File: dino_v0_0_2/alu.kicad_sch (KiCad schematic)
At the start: 20 parts, among them U38 74F382N, U40 74F382N, U45 74LS373, U46 74LS373, U47 74LS373, U48 74LS157, U49 74LS273, U50 74LS02, U52 74LS02, U53 74LS08

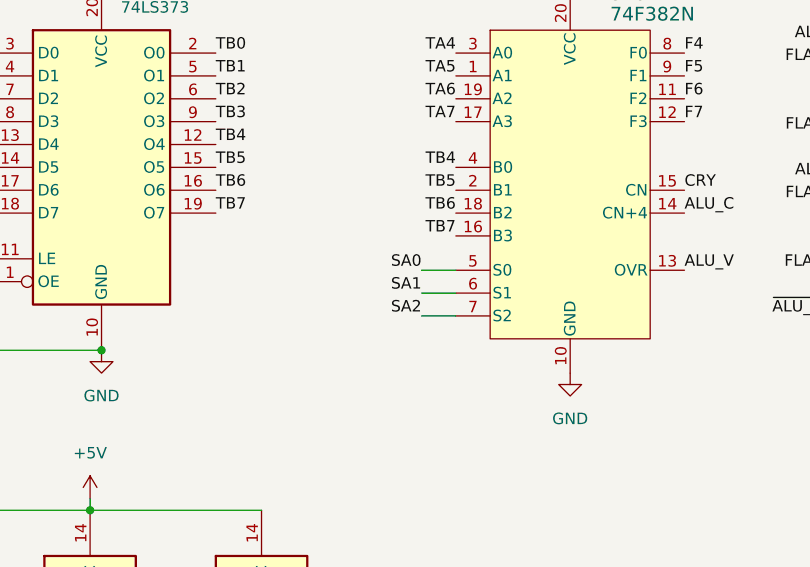
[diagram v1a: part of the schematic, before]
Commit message: schematic: join five aliased nets, and ledger the root-sheet gap
FIVE LIVE WIRES WERE IN THE CHECKLIST'S NO-CONNECT BUCKET, under the
heading "nothing to land and nothing to beep against."

  CW9/SA2           U15.12  <->  U38.7, U40.7
  CW10/SA1          U15.13  <->  U38.6, U40.6, U53.12
  CW11/SA0          U15.15  <->  U38.5, U40.5, U53.13
  CW13/PC_UP        U15.17  <->  U36.1
  CW14/PC_MAR_MUX   U15.18  <->  U54.19, U59.19, U60.11, U60.12

The microcode sheet labelled each net CWnn; the consumer sheet labelled it
SA2 / PC_UP / PC_MAR_MUX. Two label sets, two net keys, both look
sheet-local, and the cross-sheet filter drops the wire -- the M15/ROM_EN
failure, five more times.

alias_splits() could not see it. It keys on a shared BASE label, which is
how it catches CW17 vs CW17/~{SRC_BANK}. CW9 and SA2 share no substring,
so the guard was structurally blind to this shape.

Applied via kicad_gen_sheet.py ops files -- deterministic uuid5, applied
markers, valid s-expression splices -- not hand edits. Every touched sheet
reparses. dino_sheet_contracts.md is UNCHANGED, which confirms the
contracts path (hierarchical sheet pins) was always right and only the
checklist path was blind. unlanded_stubs 20 -> 14; the five now emit as
NEW: with beep partners.

Cosmetic: CW13 on program_counter sits at the same coordinate as PC_UP.
That anchor has no horizontal run, and same-point is the only placement
guaranteed to attach to the right node. Drag apart in KiCad when convenient.

A THIRD BLIND SPOT, FOUND AND LEDGERED RATHER THAN FIXED. net_pins()
walks the ten child sheets and NOT the root sheet:

    alu control_word input_output mar mdr memory microcode
    program_counter registers_a_b stack_pointer      -- no root

Root carries U6 (T-counter), U7/U8 (T decoders), U20 (divider), U27
(clock/reset), U56, U61, Y1, SW2 -- real parts on no child sheet. Their
pins can never reach a continuity checklist, and any child-sheet net
terminating on root is misreported as a no-connect. 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
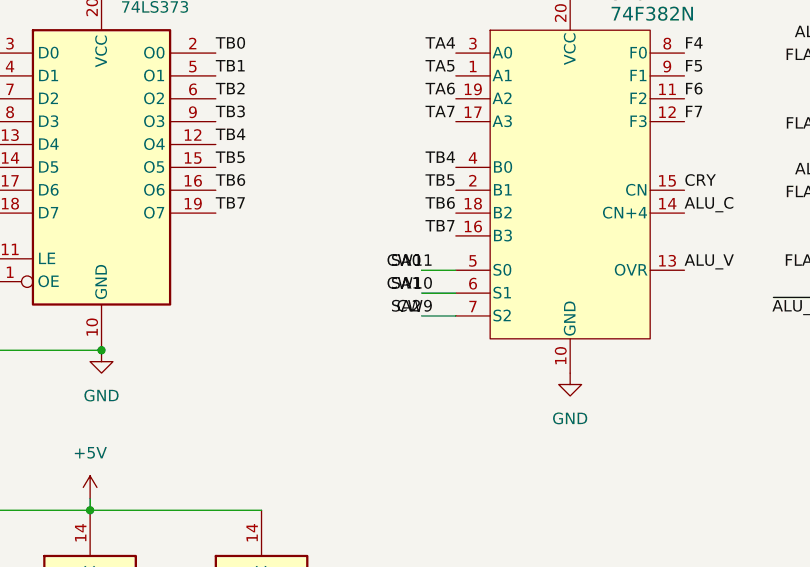
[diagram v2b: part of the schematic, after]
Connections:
- net SA0 renamed CW11
- net SA1 renamed CW10
- net SA2 renamed CW9
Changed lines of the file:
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@@
+		)
+	)
+	(label "CW9"
+		(at 142.24 119.38 180)
+		(effects
+			(font
+				(size 1.27 1.27)
+			)
+			(justify right bottom)
+		)
+	)
+	(label "CW10"
+		(at 142.24 116.84 180)
+		(effects
+			(font
+				(size 1.27 1.27)
+			)
+			(justify right bottom)
+		)
+	)
+	(label "CW11"
+		(at 142.24 114.3 180)
+		(effects
+			(font
+				(size 1.27 1.27)
+			)
+			(justify right bottom)
 		)
 	)

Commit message: feat: phase E step A -- the 16K I/O window, in schematic
Carves 0x4000-0x7FFF out of ROM space and publishes a bus. The ROM now
answers 0x0000-0x3FFF only; the window decodes to no core chip, so W
reads its park -- 0xFF, which is HALT.

TWO NEW PACKAGES, both on the memory board:

  U74 '00  ~{M14}      = NAND(M14, M14)
           ~{ROM_SEL}  = NAND(~{RAM_EN}, ~{M14})
           ~{RAM_OE_G} = NAND(RAM_OE_ON, M15)
           ~{IO_SEL}   = NAND(~{RAM_EN}, M14)
  U75 '32  ~{IO_RD}    = OR(~{IO_SEL}, READS_IDLE)
           ~{IO_WR}    = OR(~{IO_SEL}, ~{RAM_WRITE_EN})
           RESET_B     = OR(RESET, GND)
           ~{IO_RD_Q}  = OR(~{IO_RD}, CLK)

Eight copper changes: U24.20 and U22.12 to ~{ROM_SEL}, U26.22/U51.9 fed
from U74 g3, U39.10 to ~{IO_RD}, U37.10 and U28.7 unlanded, U37.11 to
GND. Park: R4-R8 + R25-R27, 4.7k on W0-7. CLK crosses through R3, 100R,
source end -- the R2 treatment.

IN RETIRES. ~{SW_OUT} has zero pins project-wide. SWITCH-GATE1's enables
are strapped +5V until card zero drives them from an address decode.

THE ROM_EN ALIAS IS DELETED. Once U24.20 moved, ROM_EN named a net with
no ROM consumer. Deleting it half-way SPLIT the net and alias_splits()
caught it mid-edit -- M15: ['M15', 'M15/ROM_EN'], the exact two-key
failure that once cost this project the ROM chip-enable on every
continuity checklist ever generated.

CLK WAS A FOURTH CROSSING THE SPEC DID NOT CARRY. Census: 15 CLK pins,
none on the memory board; ~{CLK} at U51.4 is the wrong polarity and both
new packages are full. SECTION 1's cost table predated the read-term
split that spent U75 g4, so memory is +4 and MDR is +4 -- the wire margin
is zero. Ruled: stay on memory, the output-load argument still holds.

SWITCH-GATE1/SW1/R17-R24/C48 move to their own input.kicad_sch so the
DIP card is modelled as a card. No renumbering: 168 designators
unchanged, --since reports annotate=0.

TOOLING RECONCILED TO THE DESIGN, not the reverse:
  test_continuity_completeness  M15_PINS U24.20 -> U74.10; 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
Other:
- note added: "MODULE CONTRACT — generated, do not hand-edit (kicad_contracts.py --stamp) IN: ~{ALU_OUT}, ~{REG_A_LOAD}, ~{REG_B_LOAD} <- Control Word Module IN: CW10=SA1, CW11=SA0, CW9=SA2 <- Microcode_Decoder IN: CLK, ~{CLK}, ~{RESET} <- root OUT: FLAG_Z -> Control Word Module BIDIR: W0-7 <-> Input, Memory Address Regiser, Memory Data Register, Output"
- note removed: "MODULE CONTRACT — generated, do not hand-edit (kicad_contracts.py --stamp) IN: ~{ALU_OUT}, ~{REG_A_LOAD}, ~{REG_B_LOAD} <- Control Word Module IN: CW10=SA1, CW11=SA0, CW9=SA2 <- Microcode_Decoder IN: CLK, ~{CLK}, ~{RESET} <- root OUT: FLAG_Z -> Control Word Module BIDIR: W0-7 <-> Memory Address Regiser, Memory Data Register, Output"
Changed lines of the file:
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@@
 		)
 	)
-	(text "MODULE CONTRACT — generated, do not hand-edit (kicad_contracts.py --stamp)\nIN: ~{ALU_OUT}, ~{REG_A_LOAD}, ~{REG_B_LOAD} <- Control Word Module\nIN: CW10=SA1, CW11=SA0, CW9=SA2 <- Microcode_Decoder\nIN: CLK, ~{CLK}, ~{RESET} <- root\nOUT: FLAG_Z -> Control Word Module\nBIDIR: W0-7 <-> Memory Address Regiser, Memory Data Register, Output"
+	(text "MODULE CONTRACT — generated, do not hand-edit (kicad_contracts.py --stamp)\nIN: ~{ALU_OUT}, ~{REG_A_LOAD}, ~{REG_B_LOAD} <- Control Word Module\nIN: CW10=SA1, CW11=SA0, CW9=SA2 <- Microcode_Decoder\nIN: CLK, ~{CLK}, ~{RESET} <- root\nOUT: FLAG_Z -> Control Word Module\nBIDIR: W0-7 <-> Input, Memory Address Regiser, Memory Data Register, Output"
 		(exclude_from_sim no)
 		(at 159.258 169.926 0)
